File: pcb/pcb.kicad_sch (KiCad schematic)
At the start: 8 parts, among them U1 I2C OLED DISPLAY

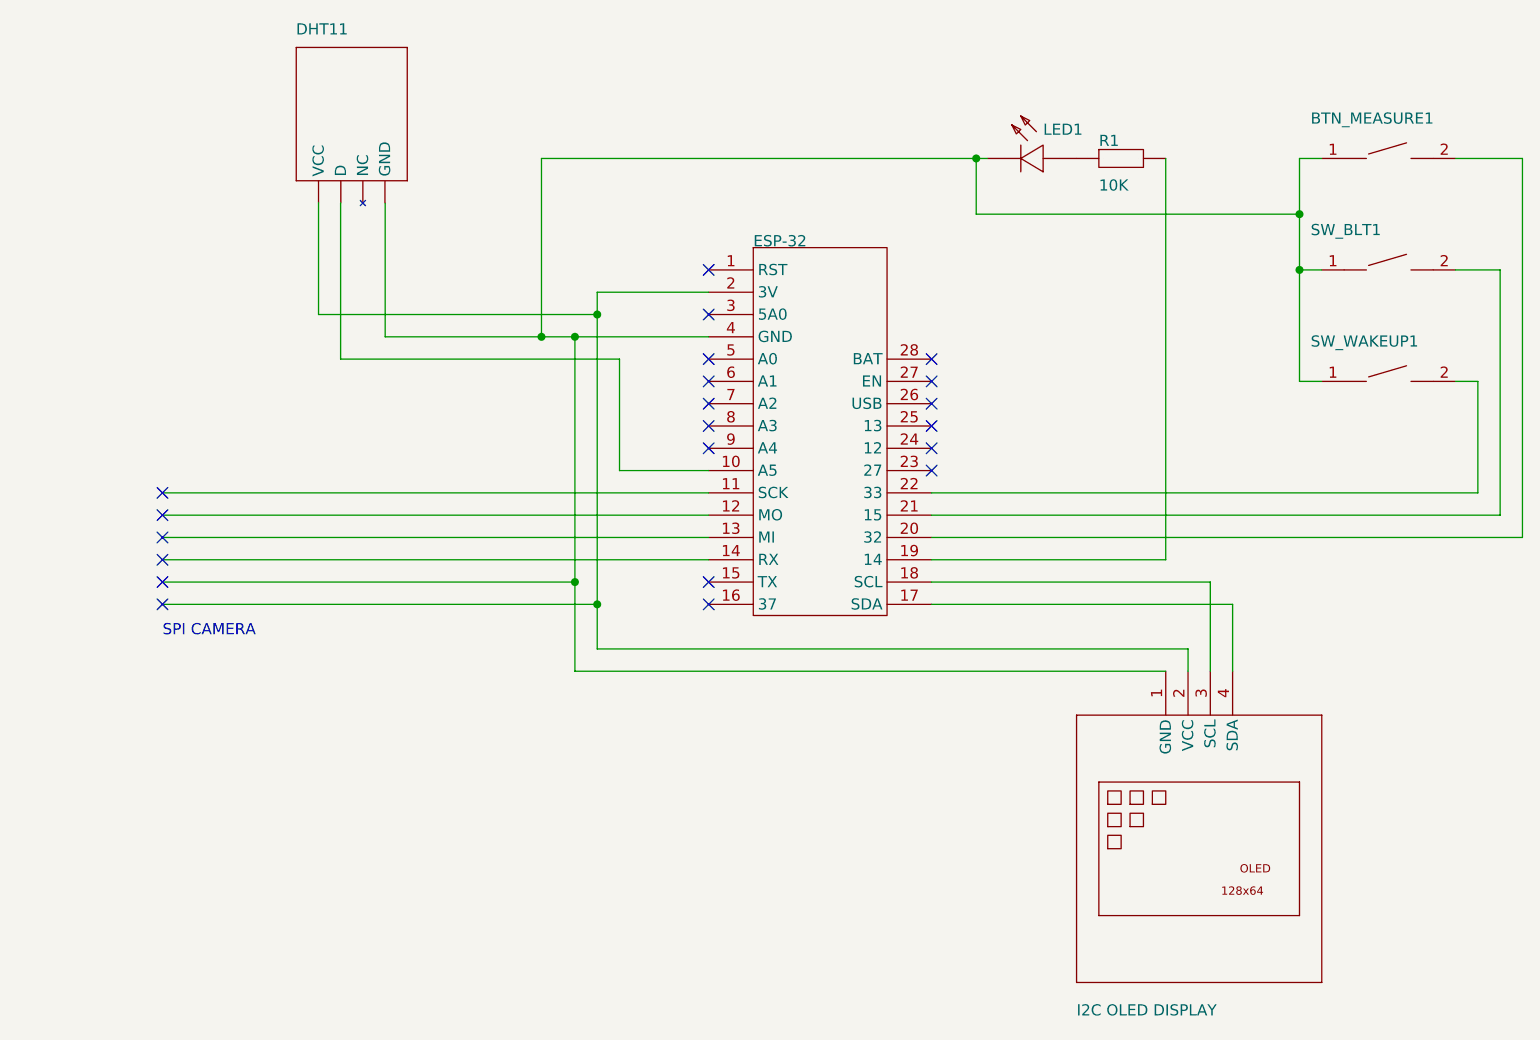
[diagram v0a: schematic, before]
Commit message: Integrated Arducam library with the rest of the code, updated PCB and schematic
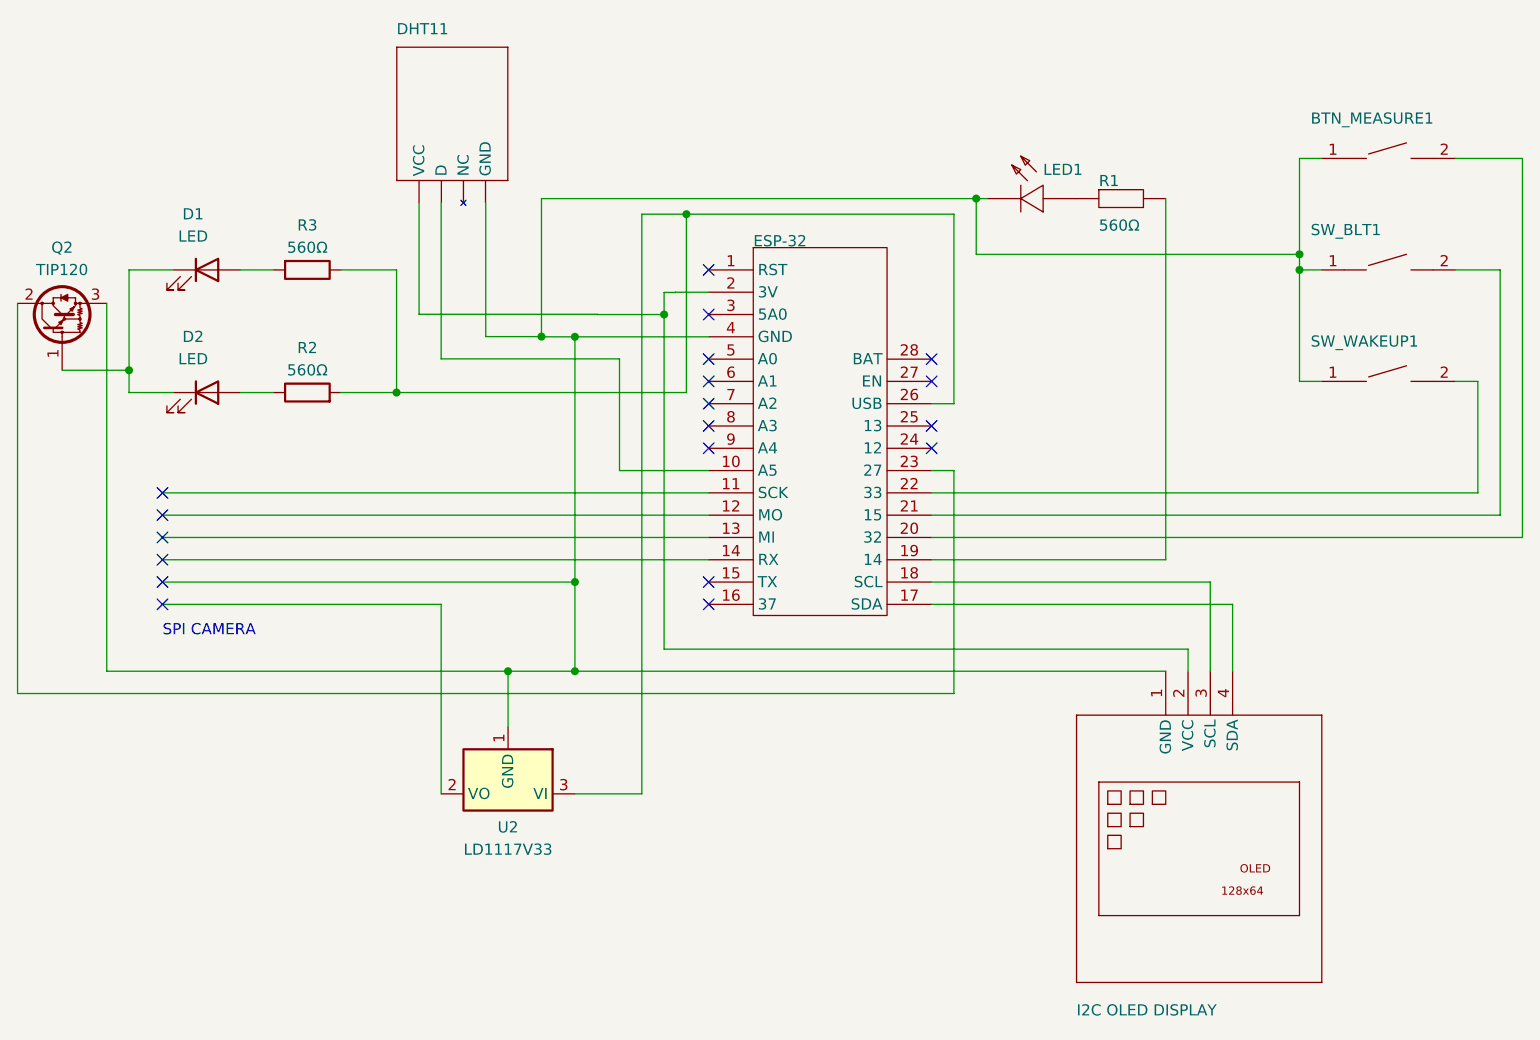
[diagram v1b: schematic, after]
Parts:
- added D1, D2: LED, symbol Device:LED
- added Q2: TIP120, Package_TO_SOT_THT:TO-220-3_Vertical, symbol Transistor_BJT:TIP120
- added R2, R3: 560Ω, symbol Device:R
- added U2: LD1117V33, Package_TO_SOT_THT:TO-220-3_Vertical, symbol Regulator_Linear:LD1117V33
- R1: value 10K -> 560Ω
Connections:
- net at BTN_MEASURE1.1, ESP-32.4 (GND), LED1.2 (C)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: now also Q2.3 (E), U2.1 (GND)
- net at DHT11. (GND): now also ESP-32.2 (3V), U1.2 (VCC)
- net at ESP-32.23 (27): now also Q2.2 (C)
- net at ESP-32.26 (USB): now also R2.2, R3.1, U2.3 (VI)
- new net: D1.1 (K), D2.1 (K), Q2.1 (B)
- new net: D1.2 (A), R3.2
- new net: D2.2 (A), R2.1
- no-connect marks 21 -> 19
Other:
- moved on the sheet: DHT11, LED1, R1
